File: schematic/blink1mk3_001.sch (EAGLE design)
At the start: 13 parts, among them U2 EFM32HG309F64G, X1 USB

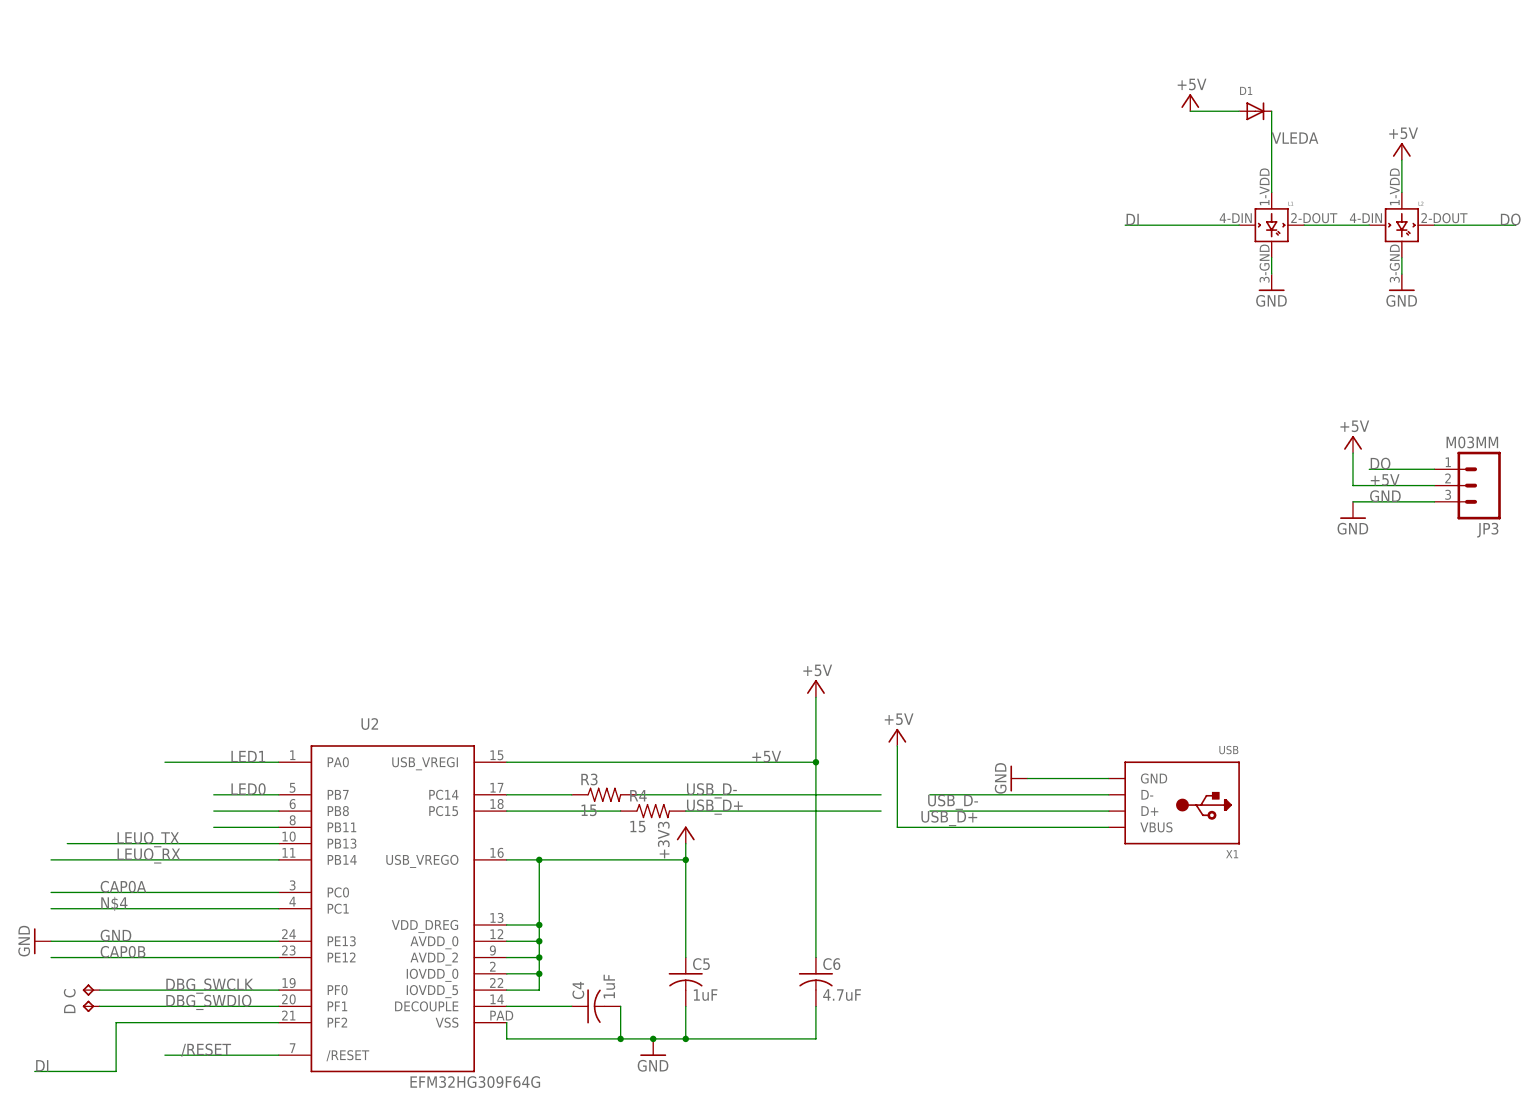
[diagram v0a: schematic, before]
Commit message: fix DI pin so it does not badly interact with tomu firmware
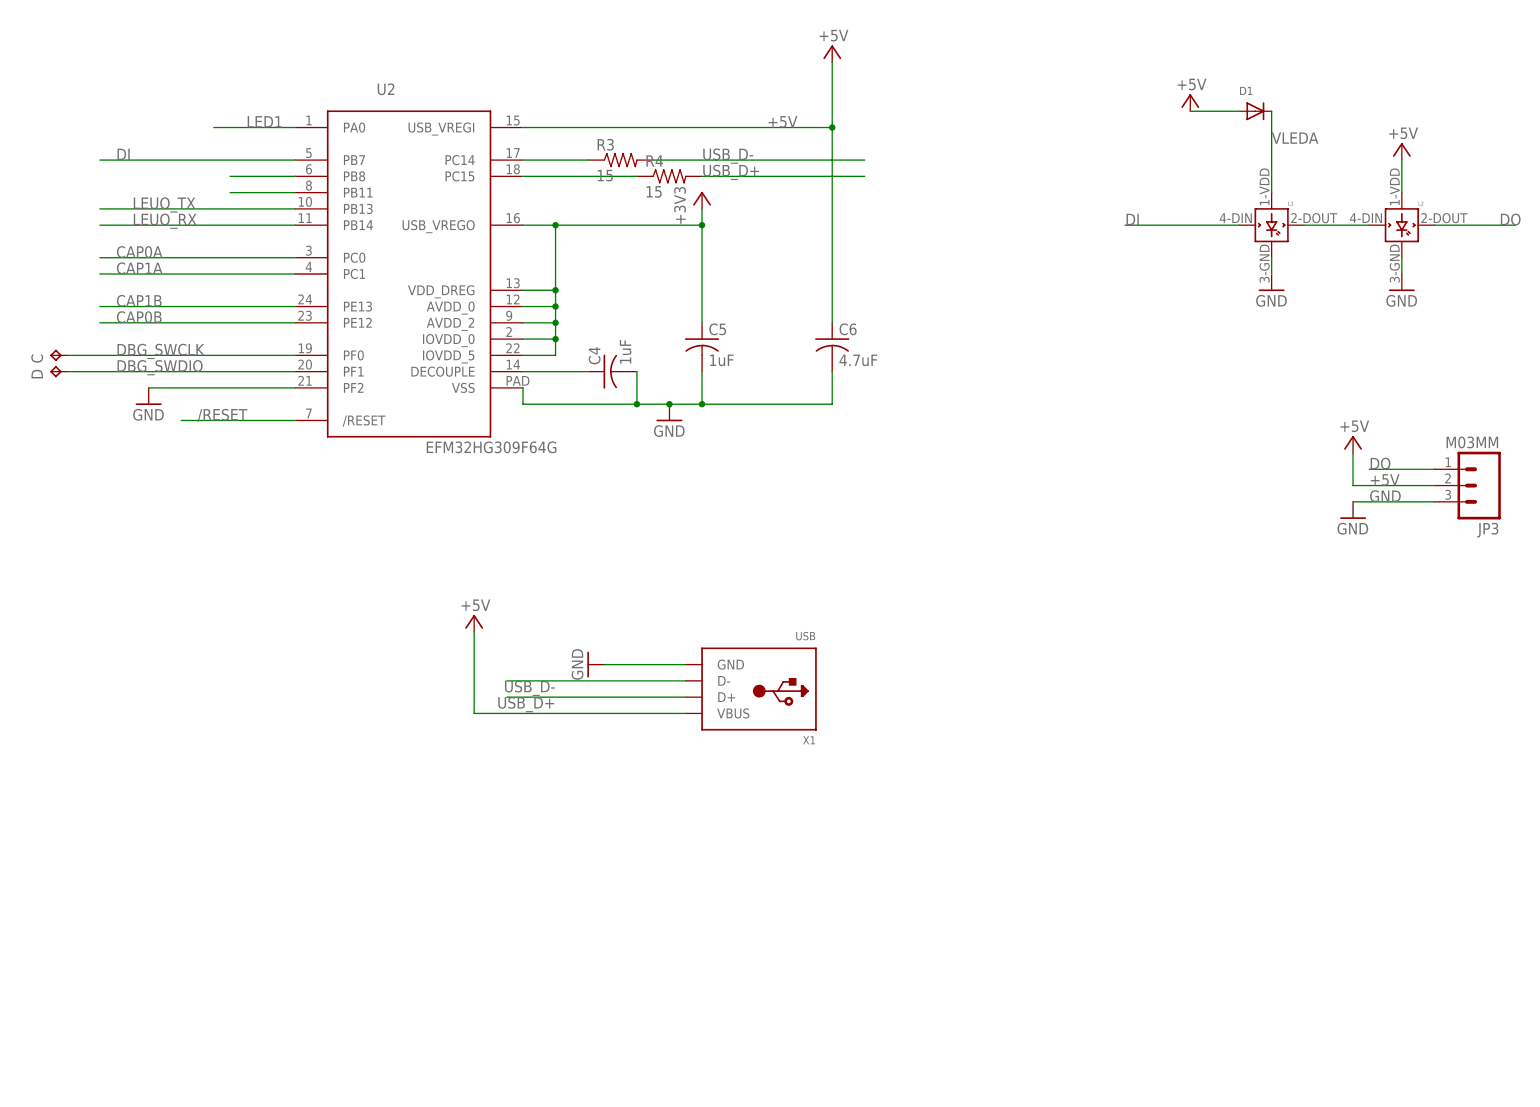
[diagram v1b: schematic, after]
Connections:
- net N$4 renamed CAP1A
- removed net LED0: U2.PB7
- new net CAP1B: U2.PE13
- net DI: now also U2.PB7; no longer U2.PF2
- net GND: now also U2.PF2; no longer U2.PE13
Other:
- moved on the sheet: C, C4, C5, C6, D, R3, R4, U2, X1

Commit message: better pcb layout
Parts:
- D1: device adafruit:DIODESOD-523 -> diode:DIODE-SOD523
- renumbered U2 to U1
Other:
- moved on the sheet: D1

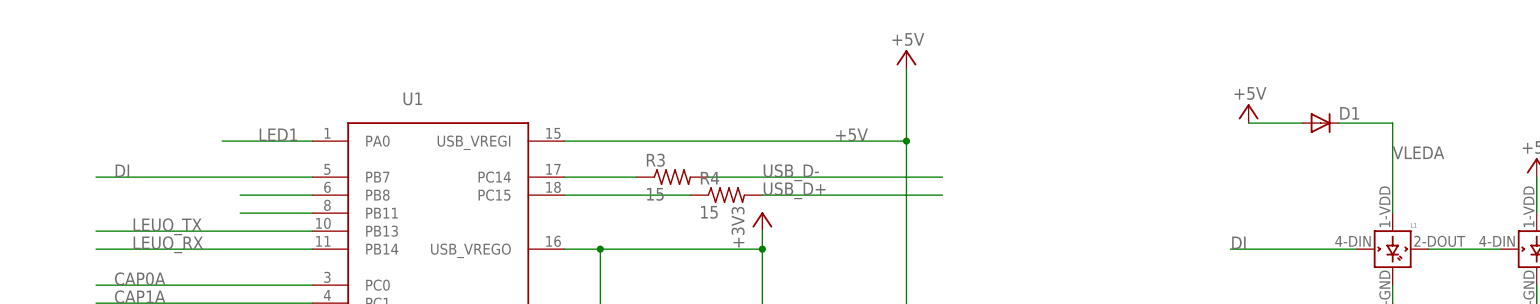
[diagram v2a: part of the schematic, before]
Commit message: version submitted to oshpark
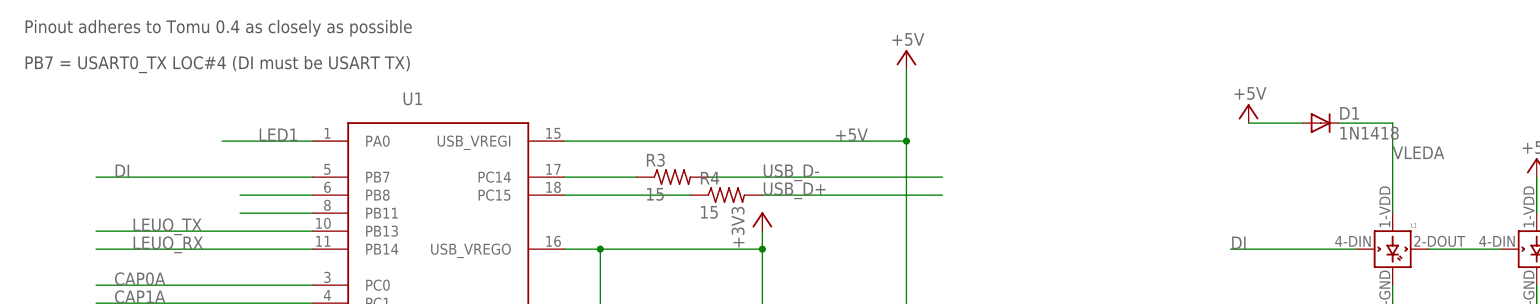
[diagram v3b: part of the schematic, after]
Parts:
- D1: value (none) -> 1N1418
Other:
- note added: "PB7 = USART0_TX LOC#4 (DI must be USART TX)"
- note added: "Pinout adheres to Tomu 0.4 as closely as possible"
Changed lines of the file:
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@@
 <part name="P+2" library="supply1" deviceset="+5V" device=""/>
 <part name="GND3" library="supply1" library_urn="urn:adsk.eagle:library:371" deviceset="GND" device=""/>
-<part name="D1" library="diode" library_urn="urn:adsk.eagle:library:210" deviceset="DIODE-" device="SOD523" package3d_urn="urn:adsk.eagle:package:43410/1"/>
+<part name="D1" library="diode" library_urn="urn:adsk.eagle:library:210" deviceset="DIODE-" device="SOD523" package3d_urn="urn:adsk.eagle:package:43410/1" value="1N1418"/>
 </parts>
 <sheets>
 <sheet>
 <plain>
+<text x="25.4" y="175.26" size="1.778" layer="97">PB7 = USART0_TX LOC#4 (DI must be USART TX)</text>
+<text x="25.4" y="180.34" size="1.778" layer="97">Pinout adheres to Tomu 0.4 as closely as possible</text>
 </plain>
 <instances>
